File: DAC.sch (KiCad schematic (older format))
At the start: 18 parts, among them U2 PCM5102

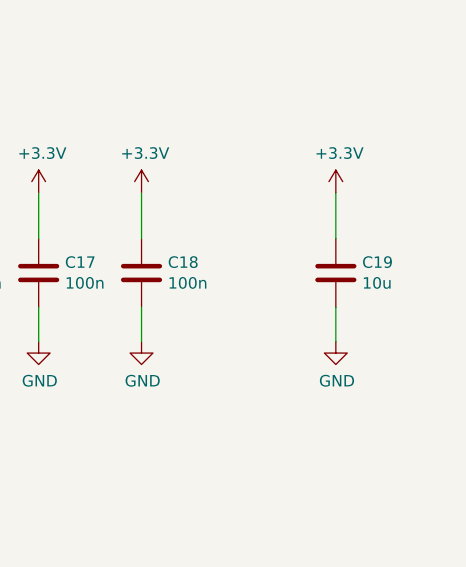
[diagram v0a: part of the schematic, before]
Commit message: selecting actual components
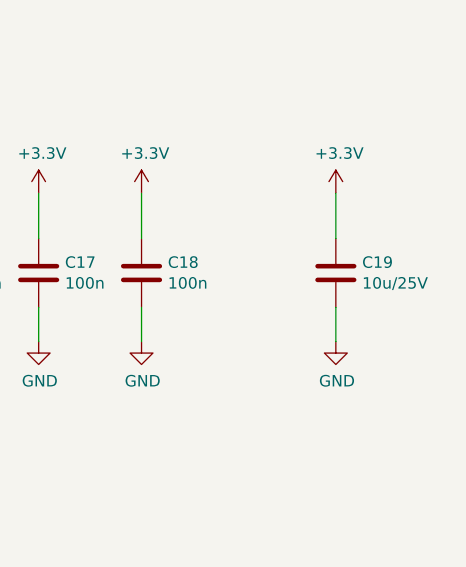
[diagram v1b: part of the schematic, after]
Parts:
- C11, C12: footprint (none) -> Capacitor_SMD:C_0603_1608Metric
- C13, C16, C17, C18: footprint Capacitor_SMD:C_0603_1608Metric -> Capacitor_SMD:C_0402_1005Metric
- C14, C15: footprint (none) -> Capacitor_SMD:C_0402_1005Metric
- C19: value 10u -> 10u/25V; footprint (none) -> Resistor_SMD:R_0805_2012Metric; PN (none) -> TMK212BBJ106MG-T
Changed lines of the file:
@@
 EESchema Schematic File Version 4
+LIBS:BalancedAudioBox-cache
 EELAYER 29 0
 EELAYER END
@@
 F 0 "C14" H 6965 3746 50  0000 L CNN
 F 1 "2.2n" H 6965 3655 50  0000 L CNN
-F 2 "" H 6888 3550 50  0001 C CNN
+F 2 "Capacitor_SMD:C_0402_1005Metric" H 6888 3550 50  0001 C CNN
 F 3 "~" H 6850 3700 50  0001 C CNN
 	1    6850 3700
@@
 F 0 "C15" H 7765 3746 50  0000 L CNN
 F 1 "2.2n" H 7765 3655 50  0000 L CNN
-F 2 "" H 7688 3550 50  0001 C CNN
+F 2 "Capacitor_SMD:C_0402_1005Metric" H 7688 3550 50  0001 C CNN
 F 3 "~" H 7650 3700 50  0001 C CNN
 	1    7650 3700
@@
 F 0 "C11" H 6315 3796 50  0000 L CNN
 F 1 "2.2u" H 6315 3705 50  0000 L CNN
-F 2 "" H 6238 3600 50  0001 C CNN
+F 2 "Capacitor_SMD:C_0603_1608Metric" H 6238 3600 50  0001 C CNN
 F 3 "~" H 6200 3750 50  0001 C CNN
 	1    6200 3750
@@
 F 0 "C12" H 6315 4496 50  0000 L CNN
 F 1 "2.2u" H 6315 4405 50  0000 L CNN
-F 2 "" H 6238 4300 50  0001 C CNN
+F 2 "Capacitor_SMD:C_0603_1608Metric" H 6238 4300 50  0001 C CNN
 F 3 "~" H 6200 4450 50  0001 C CNN
 	1    6200 4450
@@
 F 0 "C13" H 6765 4496 50  0000 L CNN
 F 1 "100n" H 6765 4405 50  0000 L CNN
-F 2 "Capacitor_SMD:C_0603_1608Metric" H 6688 4300 50  0001 C CNN
+F 2 "Capacitor_SMD:C_0402_1005Metric" H 6688 4300 50  0001 C CNN
 F 3 "~" H 6650 4450 50  0001 C CNN
 	1    6650 4450
@@
 F 0 "C16" H 9015 4346 50  0000 L CNN
 F 1 "100n" H 9015 4255 50  0000 L CNN
-F 2 "Capacitor_SMD:C_0603_1608Metric" H 8938 4150 50  0001 C CNN
+F 2 "Capacitor_SMD:C_0402_1005Metric" H 8938 4150 50  0001 C CNN
 F 3 "~" H 8900 4300 50  0001 C CNN
 	1    8900 4300
@@
 F 0 "C17" H 9465 4346 50  0000 L CNN
 F 1 "100n" H 9465 4255 50  0000 L CNN
-F 2 "Capacitor_SMD:C_0603_1608Metric" H 9388 4150 50  0001 C CNN
+F 2 "Capacitor_SMD:C_0402_1005Metric" H 9388 4150 50  0001 C CNN
 F 3 "~" H 9350 4300 50  0001 C CNN
 	1    9350 4300
@@
 F 0 "C18" H 9915 4346 50  0000 L CNN
 F 1 "100n" H 9915 4255 50  0000 L CNN
-F 2 "Capacitor_SMD:C_0603_1608Metric" H 9838 4150 50  0001 C CNN
+F 2 "Capacitor_SMD:C_0402_1005Metric" H 9838 4150 50  0001 C CNN
 F 3 "~" H 9800 4300 50  0001 C CNN
 	1    9800 4300
@@
 P 10650 4300
 F 0 "C19" H 10765 4346 50  0000 L CNN
-F 1 "10u" H 10765 4255 50  0000 L CNN
-F 2 "" H 10688 4150 50  0001 C CNN
+F 1 "10u/25V" H 10765 4255 50  0000 L CNN
+F 2 "Resistor_SMD:R_0805_2012Metric" H 10688 4150 50  0001 C CNN
 F 3 "~" H 10650 4300 50  0001 C CNN
+F 4 "TMK212BBJ106MG-T" H 10650 4300 50  0001 C CNN "PN"
 	1    10650 4300
 	1    0    0    -1

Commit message: placement complete
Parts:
- C11, C12: footprint Capacitor_SMD:C_0603_1608Metric -> Capacitor_SMD:C_0805_2012Metric
- C19: footprint Resistor_SMD:R_0805_2012Metric -> Capacitor_SMD:C_0805_2012Metric
- R10, R11, R12, R7, R8, R9: footprint Resistor_SMD:R_0603_1608Metric -> Resistor_SMD:R_0402_1005Metric
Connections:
- net +3V3: now also R7.1
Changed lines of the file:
@@
 F 0 "R10" V 6343 3400 50  0000 C CNN
 F 1 "1k" V 6434 3400 50  0000 C CNN
-F 2 "Resistor_SMD:R_0603_1608Metric" V 6480 3400 50  0001 C CNN
+F 2 "Resistor_SMD:R_0402_1005Metric" V 6480 3400 50  0001 C CNN
 F 3 "~" H 6550 3400 50  0001 C CNN
 	1    6550 3400
@@
 F 0 "R9" V 6343 3100 50  0000 C CNN
 F 1 "1k" V 6434 3100 50  0000 C CNN
-F 2 "Resistor_SMD:R_0603_1608Metric" V 6480 3100 50  0001 C CNN
+F 2 "Resistor_SMD:R_0402_1005Metric" V 6480 3100 50  0001 C CNN
 F 3 "~" H 6550 3100 50  0001 C CNN
 	1    6550 3100
@@
 F 0 "C11" H 6315 3796 50  0000 L CNN
 F 1 "2.2u" H 6315 3705 50  0000 L CNN
-F 2 "Capacitor_SMD:C_0603_1608Metric" H 6238 3600 50  0001 C CNN
+F 2 "Capacitor_SMD:C_0805_2012Metric" H 6238 3600 50  0001 C CNN
 F 3 "~" H 6200 3750 50  0001 C CNN
 	1    6200 3750
@@
 F 0 "C12" H 6315 4496 50  0000 L CNN
 F 1 "2.2u" H 6315 4405 50  0000 L CNN
-F 2 "Capacitor_SMD:C_0603_1608Metric" H 6238 4300 50  0001 C CNN
+F 2 "Capacitor_SMD:C_0805_2012Metric" H 6238 4300 50  0001 C CNN
 F 3 "~" H 6200 4450 50  0001 C CNN
 	1    6200 4450
@@
 F 0 "R11" H 7320 3746 50  0000 L CNN
 F 1 "1k" H 7320 3655 50  0000 L CNN
-F 2 "Resistor_SMD:R_0603_1608Metric" V 7180 3700 50  0001 C CNN
+F 2 "Resistor_SMD:R_0402_1005Metric" V 7180 3700 50  0001 C CNN
 F 3 "~" H 7250 3700 50  0001 C CNN
 	1    7250 3700
@@
 F 0 "R12" H 8120 3746 50  0000 L CNN
 F 1 "1k" H 8120 3655 50  0000 L CNN
-F 2 "Resistor_SMD:R_0603_1608Metric" V 7980 3700 50  0001 C CNN
+F 2 "Resistor_SMD:R_0402_1005Metric" V 7980 3700 50  0001 C CNN
 F 3 "~" H 8050 3700 50  0001 C CNN
 	1    8050 3700
@@
 F 0 "C19" H 10765 4346 50  0000 L CNN
 F 1 "10u/25V" H 10765 4255 50  0000 L CNN
-F 2 "Resistor_SMD:R_0805_2012Metric" H 10688 4150 50  0001 C CNN
+F 2 "Capacitor_SMD:C_0805_2012Metric" H 10688 4150 50  0001 C CNN
 F 3 "~" H 10650 4300 50  0001 C CNN
 F 4 "TMK212BBJ106MG-T" H 10650 4300 50  0001 C CNN "PN"
@@
 F 0 "R8" H 3270 4396 50  0000 L CNN
 F 1 "2k7" H 3270 4305 50  0000 L CNN
-F 2 "Resistor_SMD:R_0603_1608Metric" V 3130 4350 50  0001 C CNN
+F 2 "Resistor_SMD:R_0402_1005Metric" V 3130 4350 50  0001 C CNN
 F 3 "~" H 3200 4350 50  0001 C CNN
 	1    3200 4350
@@
 F 0 "R7" H 3270 3796 50  0000 L CNN
 F 1 "7k5" H 3270 3705 50  0000 L CNN
-F 2 "Resistor_SMD:R_0603_1608Metric" V 3130 3750 50  0001 C CNN
+F 2 "Resistor_SMD:R_0402_1005Metric" V 3130 3750 50  0001 C CNN
 F 3 "~" H 3200 3750 50  0001 C CNN
 	1    3200 3750
@@
 Text Notes 2650 4050 0    50   ~ 0
 mute=2V
+$Comp
+L power:+3.3V #PWR078
+U 1 1 5D46695C
+P 3200 3250
+F 0 "#PWR078" H 3200 3100 50  0001 C CNN
+F 1 "+3.3V" H 3215 3423 50  0000 C CNN
+F 2 "" H 3200 3250 50  0001 C CNN
+F 3 "" H 3200 3250 50  0001 C CNN
+	1    3200 3250
+	1    0    0    -1
+$EndComp
 $EndSCHEMATC

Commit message: layout and silk
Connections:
- net DEEMP: now reaches JP2.2 (C), U2.10 (DEMP)
- net LATENCY: now reaches JP1.2 (C), U2.11 (FLT)
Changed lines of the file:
@@
 	1    0    0    -1
 $EndComp
+Text Label 4350 4350 0    50   ~ 0
+DEEMP
+Text Label 4500 3800 0    50   ~ 0
+LATENCY
 $EndSCHEMATC

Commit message: adding regulator
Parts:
- added U3: AP1117-33, Package_TO_SOT_SMD:SOT-223-3_TabPin2, symbol Regulator_Linear:AP1117-33
- R7: value 7k5 -> 2k2
- R8: value 2k7 -> 3k3
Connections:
- net +3V3: no longer C18.1, C19.1, R7.1, U2.8 (AVDD)
- net GND: now also U3.1 (GND)
- new net +3.3VA: C18.1, C19.1, U2.8 (AVDD), U3.2 (VO)
- new net VIN: R7.1
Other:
- note added: "5.5V to 3.3V"
- note added: "minimum VIN 3.3V"
- moved on the sheet: C18
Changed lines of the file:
@@
 Wire Wire Line
 	5350 2900 5450 2900
-Connection ~ 5450 2900
-Wire Wire Line
-	5550 3100 5550 2900
-Wire Wire Line
-	5550 2900 5450 2900
 Text HLabel 4750 3300 0    50   Input ~ 0
 LRCLK
@@
 L Device:C C18
 U 1 1 5D42884D
-P 9800 4300
-F 0 "C18" H 9915 4346 50  0000 L CNN
-F 1 "100n" H 9915 4255 50  0000 L CNN
-F 2 "Capacitor_SMD:C_0402_1005Metric" H 9838 4150 50  0001 C CNN
-F 3 "~" H 9800 4300 50  0001 C CNN
-	1    9800 4300
+P 10200 4300
+F 0 "C18" H 10315 4346 50  0000 L CNN
+F 1 "100n" H 10315 4255 50  0000 L CNN
+F 2 "Capacitor_SMD:C_0402_1005Metric" H 10238 4150 50  0001 C CNN
+F 3 "~" H 10200 4300 50  0001 C CNN
+	1    10200 4300
 	1    0    0    -1
 $EndComp
@@
 $EndComp
 $Comp
-L power:+3.3V #PWR045
-U 1 1 5D42AAB2
-P 9800 3950
-F 0 "#PWR045" H 9800 3800 50  0001 C CNN
-F 1 "+3.3V" H 9815 4123 50  0000 C CNN
-F 2 "" H 9800 3950 50  0001 C CNN
-F 3 "" H 9800 3950 50  0001 C CNN
-	1    9800 3950
-	1    0    0    -1
-$EndComp
-$Comp
 L power:GND #PWR042
 U 1 1 5D42ADA2
@@
 L power:GND #PWR046
 U 1 1 5D42B3EB
-P 9800 4600
-F 0 "#PWR046" H 9800 4350 50  0001 C CNN
-F 1 "GND" H 9805 4427 50  0000 C CNN
-F 2 "" H 9800 4600 50  0001 C CNN
-F 3 "" H 9800 4600 50  0001 C CNN
-	1    9800 4600
+P 10200 4600
+F 0 "#PWR046" H 10200 4350 50  0001 C CNN
+F 1 "GND" H 10205 4427 50  0000 C CNN
+F 2 "" H 10200 4600 50  0001 C CNN
+F 3 "" H 10200 4600 50  0001 C CNN
+	1    10200 4600
 	1    0    0    -1
 $EndComp
@@
 	9350 4600 9350 4450
 Wire Wire Line
-	9800 4600 9800 4450
+	10200 4600 10200 4450
 Wire Wire Line
 	9350 4150 9350 3950
 Wire Wire Line
 	8900 4150 8900 3950
-Wire Wire Line
-	9800 4150 9800 3950
 Wire Wire Line
 	6700 3100 7650 3100
@@
 $EndComp
 $Comp
-L power:+3.3V #PWR047
-U 1 1 5D43D315
-P 10650 3950
-F 0 "#PWR047" H 10650 3800 50  0001 C CNN
-F 1 "+3.3V" H 10665 4123 50  0000 C CNN
-F 2 "" H 10650 3950 50  0001 C CNN
-F 3 "" H 10650 3950 50  0001 C CNN
-	1    10650 3950
-	1    0    0    -1
-$EndComp
-$Comp
 L power:GND #PWR048
 U 1 1 5D43D31B
@@
 	10650 4600 10650 4450
 Wire Wire Line
-	10650 4150 10650 3950
-Wire Wire Line
 	4750 3300 4950 3300
 Wire Wire Line
@@
 P 3200 4350
 F 0 "R8" H 3270 4396 50  0000 L CNN
-F 1 "2k7" H 3270 4305 50  0000 L CNN
+F 1 "3k3" H 3270 4305 50  0000 L CNN
 F 2 "Resistor_SMD:R_0402_1005Metric" V 3130 4350 50  0001 C CNN
 F 3 "~" H 3200 4350 50  0001 C CNN
@@
 P 3200 3750
 F 0 "R7" H 3270 3796 50  0000 L CNN
-F 1 "7k5" H 3270 3705 50  0000 L CNN
+F 1 "2k2" H 3270 3705 50  0000 L CNN
 F 2 "Resistor_SMD:R_0402_1005Metric" V 3130 3750 50  0001 C CNN
 F 3 "~" H 3200 3750 50  0001 C CNN
@@
 	0    -1   -1   0
 $EndComp
-Wire Wire Line
-	5450 2900 5450 2800
 $Comp
 L power:+3.3V #PWR033
 U 1 1 5D41F899
-P 5450 2800
-F 0 "#PWR033" H 5450 2650 50  0001 C CNN
-F 1 "+3.3V" H 5465 2973 50  0000 C CNN
-F 2 "" H 5450 2800 50  0001 C CNN
-F 3 "" H 5450 2800 50  0001 C CNN
-	1    5450 2800
+P 5350 2800
+F 0 "#PWR033" H 5350 2650 50  0001 C CNN
+F 1 "+3.3V" H 5365 2973 50  0000 C CNN
+F 2 "" H 5350 2800 50  0001 C CNN
+F 3 "" H 5350 2800 50  0001 C CNN
+	1    5350 2800
 	1    0    0    -1
 $EndComp
@@
 Text Notes 2650 4050 0    50   ~ 0
 mute=2V
-$Comp
-L power:+3.3V #PWR078
-U 1 1 5D46695C
-P 3200 3250
-F 0 "#PWR078" H 3200 3100 50  0001 C CNN
-F 1 "+3.3V" H 3215 3423 50  0000 C CNN
-F 2 "" H 3200 3250 50  0001 C CNN
-F 3 "" H 3200 3250 50  0001 C CNN
-	1    3200 3250
-	1    0    0    -1
-$EndComp
 Text Label 4350 4350 0    50   ~ 0
 DEEMP
 Text Label 4500 3800 0    50   ~ 0
 LATENCY
+Text GLabel 3200 3250 1    50   Input ~ 0
+VIN
+Text Notes 2600 4200 0    50   ~ 0
+5.5V to 3.3V
+Text Notes 2350 4350 0    50   ~ 0
+minimum VIN 3.3V
+Wire Wire Line
+	5350 2800 5350 2900
+Connection ~ 5350 2900
+$Comp
+L power:+3.3VA #PWR045
+U 1 1 5D44A10E
+P 5550 2500
+F 0 "#PWR045" H 5550 2350 50  0001 C CNN
+F 1 "+3.3VA" H 5565 2673 50  0000 C CNN
+F 2 "" H 5550 2500 50  0001 C CNN
+F 3 "" H 5550 2500 50  0001 C CNN
+	1    5550 2500
+	1    0    0    -1
+$EndComp
+Wire Wire Line
+	5550 2500 5550 3100
+$Comp
+L power:+3.3VA #PWR080
+U 1 1 5D44C07E
+P 10650 3900
+F 0 "#PWR080" H 10650 3750 50  0001 C CNN
+F 1 "+3.3VA" H 10665 4073 50  0000 C CNN
+F 2 "" H 10650 3900 50  0001 C CNN
+F 3 "" H 10650 3900 50  0001 C CNN
+	1    10650 3900
+	1    0    0    -1
+$EndComp
+$Comp
+L power:+3.3VA #PWR078
+U 1 1 5D44C719
+P 10200 3900
+F 0 "#PWR078" H 10200 3750 50  0001 C CNN
+F 1 "+3.3VA" H 10215 4073 50  0000 C CNN
+F 2 "" H 10200 3900 50  0001 C CNN
+F 3 "" H 10200 3900 50  0001 C CNN
+	1    10200 3900
+	1    0    0    -1
+$EndComp
+Wire Wire Line
+	10200 3900 10200 4150
+Wire Wire Line
+	10650 3900 10650 4150
+$Comp
+L Regulator_Linear:AP1117-33 U3
+U 1 1 5D456577
+P 10050 2350
+F 0 "U3" H 10050 2592 50  0000 C CNN
+F 1 "AP1117-33" H 10050 2501 50  0000 C CNN
+F 2 "Package_TO_SOT_SMD:SOT-223-3_TabPin2" H 10050 2550 50  0001 C CNN
+F 3 "http://www.diodes.com/datasheets/AP1117.pdf" H 10150 2100 50  0001 C CNN
+	1    10050 2350
+	1    0    0    -1
+$EndComp
+$Comp
+L power:GND #PWR047
+U 1 1 5D457C9B
+P 10050 2750
+F 0 "#PWR047" H 10050 2500 50  0001 C CNN
+F 1 "GND" H 10055 2577 50  0000 C CNN
+F 2 "" H 10050 2750 50  0001 C CNN
+F 3 "" H 10050 2750 50  0001 C CNN
+	1    10050 2750
+	1    0    0    -1
+$EndComp
+$Comp
+L power:+3.3VA #PWR079
+U 1 1 5D457FEA
+P 10550 2350
+F 0 "#PWR079" H 10550 2200 50  0001 C CNN
+F 1 "+3.3VA" V 10565 2478 50  0000 L CNN
+F 2 "" H 10550 2350 50  0001 C CNN
+F 3 "" H 10550 2350 50  0001 C CNN
+	1    10550 2350
+	0    1    1    0
+$EndComp
+Wire Wire Line
+	10050 2650 10050 2750
+Wire Wire Line
+	10350 2350 10550 2350
 $EndSCHEMATC

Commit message: more layout
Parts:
- added JP4: SolderJumper_3_Bridged12, Jumper:SolderJumper-3_P1.3mm_Bridged12_Pad1.0x1.5mm, symbol Jumper:SolderJumper_3_Bridged12
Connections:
- net +3.3VA: now also C17.1, U2.1 (CPVDD)
- net +3V3: no longer C17.1, U2.1 (CPVDD)
- net VIN: now also JP4.3 (B)
- net at U3.3 (VI): now also JP4.2 (C)
- new net VOUT-5.4V: JP4.1 (A)
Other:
- moved on the sheet: C17
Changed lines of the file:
@@
 Wire Wire Line
 	5450 3100 5450 2900
-Wire Wire Line
-	5350 3100 5350 2900
-Wire Wire Line
-	5350 2900 5450 2900
 Text HLabel 4750 3300 0    50   Input ~ 0
 LRCLK
@@
 L Device:C C17
 U 1 1 5D4285E4
-P 9350 4300
-F 0 "C17" H 9465 4346 50  0000 L CNN
-F 1 "100n" H 9465 4255 50  0000 L CNN
-F 2 "Capacitor_SMD:C_0402_1005Metric" H 9388 4150 50  0001 C CNN
-F 3 "~" H 9350 4300 50  0001 C CNN
-	1    9350 4300
+P 9750 4300
+F 0 "C17" H 9865 4346 50  0000 L CNN
+F 1 "100n" H 9865 4255 50  0000 L CNN
+F 2 "Capacitor_SMD:C_0402_1005Metric" H 9788 4150 50  0001 C CNN
+F 3 "~" H 9750 4300 50  0001 C CNN
+	1    9750 4300
 	1    0    0    -1
 $EndComp
@@
 	6650 4650 6650 4600
 $Comp
-L power:+3.3V #PWR043
-U 1 1 5D429F10
-P 9350 3950
-F 0 "#PWR043" H 9350 3800 50  0001 C CNN
-F 1 "+3.3V" H 9365 4123 50  0000 C CNN
-F 2 "" H 9350 3950 50  0001 C CNN
-F 3 "" H 9350 3950 50  0001 C CNN
-	1    9350 3950
-	1    0    0    -1
-$EndComp
-$Comp
 L power:+3.3V #PWR041
 U 1 1 5D42A68C
@@
 L power:GND #PWR044
 U 1 1 5D42B0CE
-P 9350 4600
-F 0 "#PWR044" H 9350 4350 50  0001 C CNN
-F 1 "GND" H 9355 4427 50  0000 C CNN
-F 2 "" H 9350 4600 50  0001 C CNN
-F 3 "" H 9350 4600 50  0001 C CNN
-	1    9350 4600
+P 9750 4600
+F 0 "#PWR044" H 9750 4350 50  0001 C CNN
+F 1 "GND" H 9755 4427 50  0000 C CNN
+F 2 "" H 9750 4600 50  0001 C CNN
+F 3 "" H 9750 4600 50  0001 C CNN
+	1    9750 4600
 	1    0    0    -1
 $EndComp
@@
 	8900 4600 8900 4450
 Wire Wire Line
-	9350 4600 9350 4450
+	9750 4600 9750 4450
 Wire Wire Line
 	10200 4600 10200 4450
-Wire Wire Line
-	9350 4150 9350 3950
 Wire Wire Line
 	8900 4150 8900 3950
@@
 L power:+3.3V #PWR033
 U 1 1 5D41F899
-P 5350 2800
-F 0 "#PWR033" H 5350 2650 50  0001 C CNN
-F 1 "+3.3V" H 5365 2973 50  0000 C CNN
-F 2 "" H 5350 2800 50  0001 C CNN
-F 3 "" H 5350 2800 50  0001 C CNN
-	1    5350 2800
+P 5450 2900
+F 0 "#PWR033" H 5450 2750 50  0001 C CNN
+F 1 "+3.3V" H 5465 3073 50  0000 C CNN
+F 2 "" H 5450 2900 50  0001 C CNN
+F 3 "" H 5450 2900 50  0001 C CNN
+	1    5450 2900
 	1    0    0    -1
 $EndComp
@@
 Text Notes 2350 4350 0    50   ~ 0
 minimum VIN 3.3V
-Wire Wire Line
-	5350 2800 5350 2900
-Connection ~ 5350 2900
 $Comp
 L power:+3.3VA #PWR045
@@
 $EndComp
 Wire Wire Line
-	5550 2500 5550 3100
+	5550 2500 5550 2550
 $Comp
 L power:+3.3VA #PWR080
@@
 Wire Wire Line
 	10350 2350 10550 2350
+Wire Wire Line
+	5350 3100 5350 2550
+Wire Wire Line
+	5350 2550 5550 2550
+Connection ~ 5550 2550
+Wire Wire Line
+	5550 2550 5550 3100
+$Comp
+L power:+3.3VA #PWR0104
+U 1 1 5D48751F
+P 9750 3900
+F 0 "#PWR0104" H 9750 3750 50  0001 C CNN
+F 1 "+3.3VA" H 9765 4073 50  0000 C CNN
+F 2 "" H 9750 3900 50  0001 C CNN
+F 3 "" H 9750 3900 50  0001 C CNN
+	1    9750 3900
+	1    0    0    -1
+$EndComp
+Wire Wire Line
+	9750 3900 9750 4150
+$Comp
+L Jumper:SolderJumper_3_Bridged12 JP4
+U 1 1 5D497685
+P 9450 2350
+F 0 "JP4" V 9496 2418 50  0000 L CNN
+F 1 "SolderJumper_3_Bridged12" V 9405 2418 50  0000 L CNN
+F 2 "Jumper:SolderJumper-3_P1.3mm_Bridged12_Pad1.0x1.5mm" H 9450 2350 50  0001 C CNN
+F 3 "~" H 9450 2350 50  0001 C CNN
+	1    9450 2350
+	0    -1   -1   0
+$EndComp
+Text GLabel 9450 1950 1    50   Input ~ 0
+VIN
+Wire Wire Line
+	9450 2150 9450 1950
+Wire Wire Line
+	9600 2350 9750 2350
+Text GLabel 9450 2700 3    50   Input ~ 0
+VOUT-5.4V
+Wire Wire Line
+	9450 2700 9450 2550
 $EndSCHEMATC
